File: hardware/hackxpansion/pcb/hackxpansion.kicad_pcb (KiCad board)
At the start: 4 copper layers, 52 x 65 mm, 101 parts, among them CN1 533981471, CN2 533981471, CN3 533981471, CN4 533981471, IC1 ADS7128IRTET, J1 Conn_01x03_MountingPin, J2 USB_C_Receptacle_USB2.0_14P, Q1 BSS138, Q2 2N7002, SW1 SW_Push, SW2 SW_Push, SW3 SW_On_Off, U2 RP2354B, U5 SPX3819M5-L-3-3, U7 BQ24075RGT, U8 USBLC6-2SC6, Y1 ABM8-272-T3

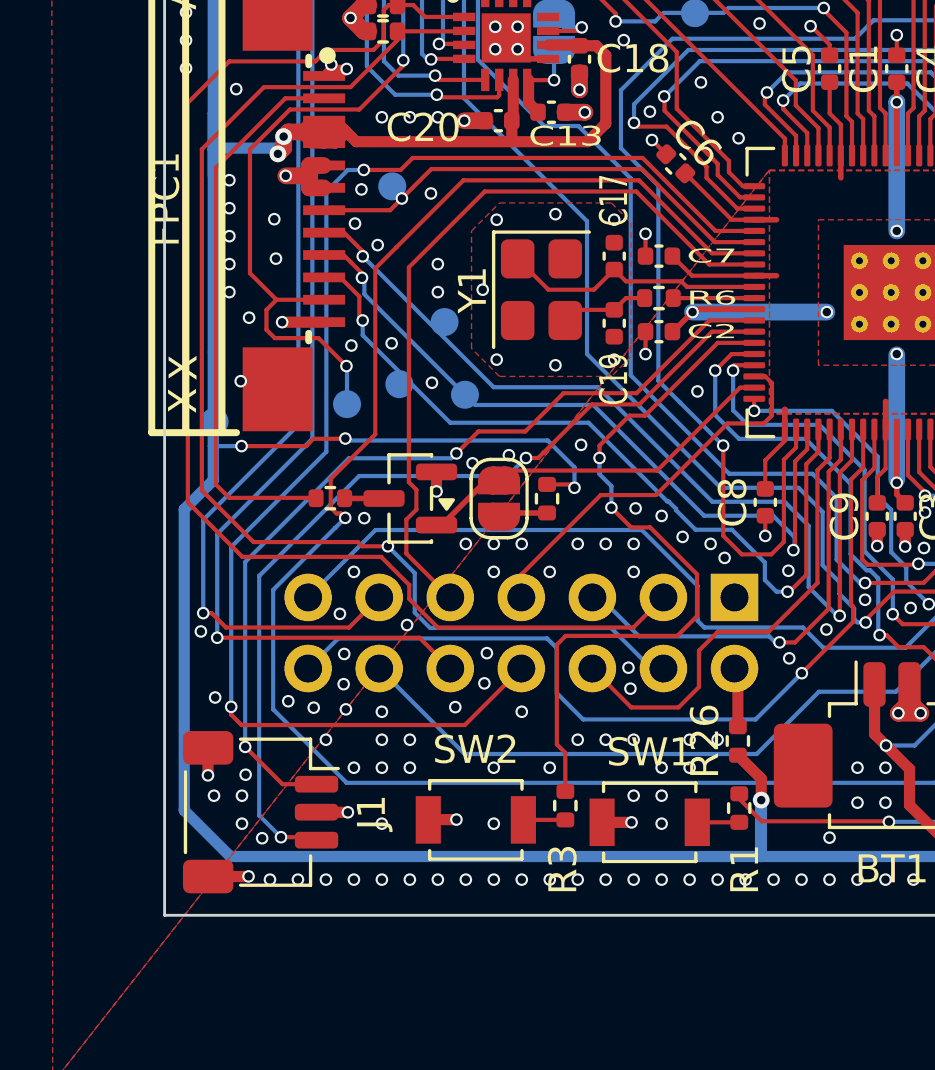
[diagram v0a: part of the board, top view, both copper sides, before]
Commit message: updated debug connector to standard 2x5 1.27mm
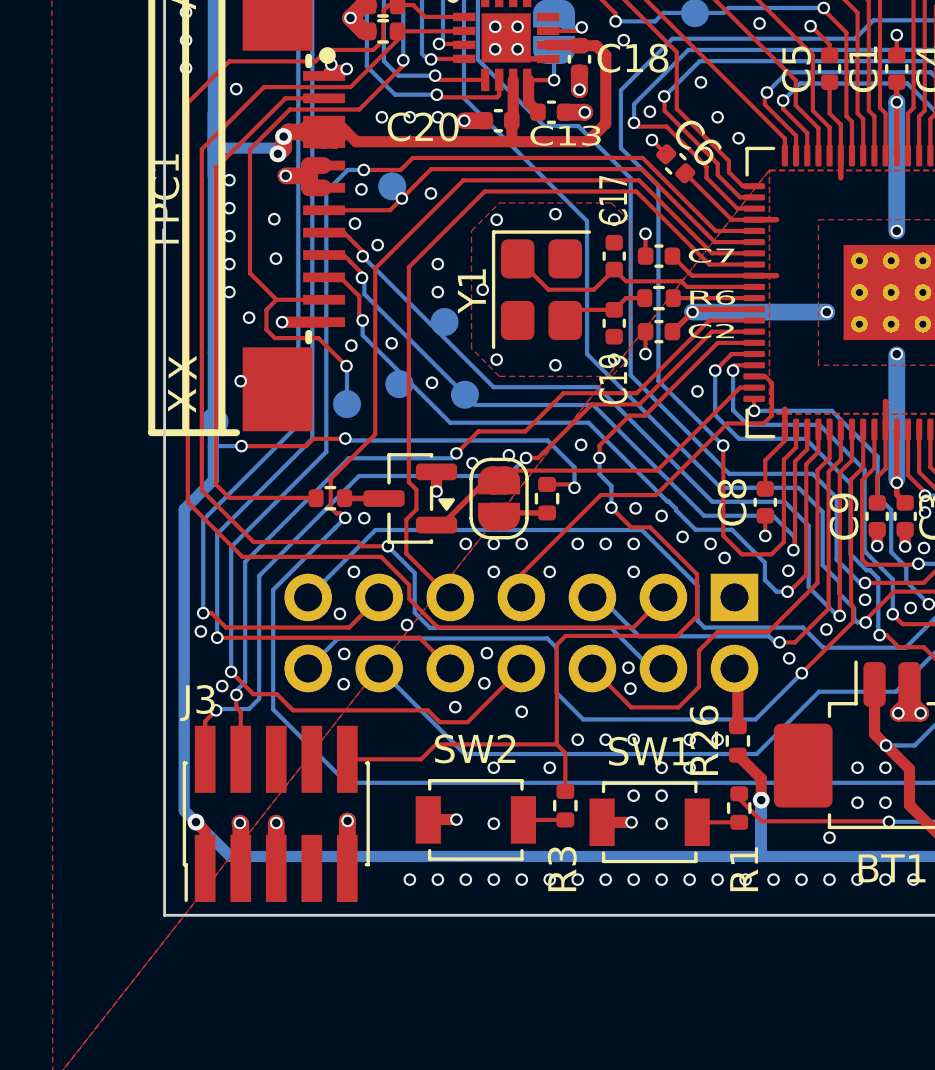
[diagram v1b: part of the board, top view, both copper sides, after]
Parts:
- removed J1: Conn_01x03_MountingPin, Connector_JST:JST_SH_SM03B-SRSS-TB_1x03-1MP_P1.00mm_Horizontal
- added J3: Conn_ARM_JTAG_SWD_10, Connector_PinHeader_1.27mm:PinHeader_2x05_P1.27mm_Vertical_SMD, F.Cu at (105.9, 97.3)
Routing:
- net /Main Board/RP2354B/RUN: track 25.8 -> 33.5 mm
- net /Main Board/RP2354B/SWDIO: track 32.3 -> 29.3 mm
- net /Main Board/RP2354B/SWCLK: track 31.5 -> 29.0 mm
- net /+3V3: track 295.6 -> 297.4 mm, vias 15 -> 16
- net /GND: track 64.4 -> 65.8 mm, vias 438 -> 417
- net /Main Board/Module Bay 0/GPIO3: track 48.3 -> 47.4 mm

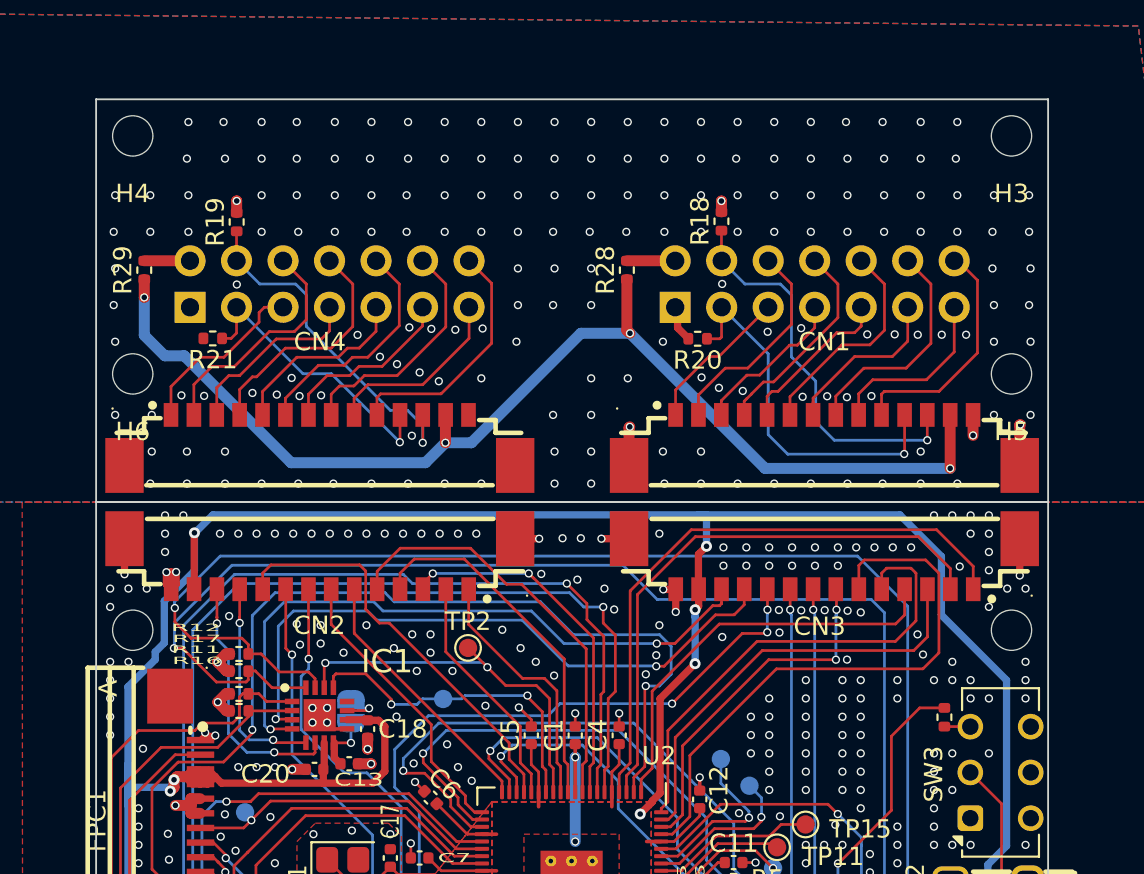
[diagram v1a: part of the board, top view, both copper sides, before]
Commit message: added silkscreen
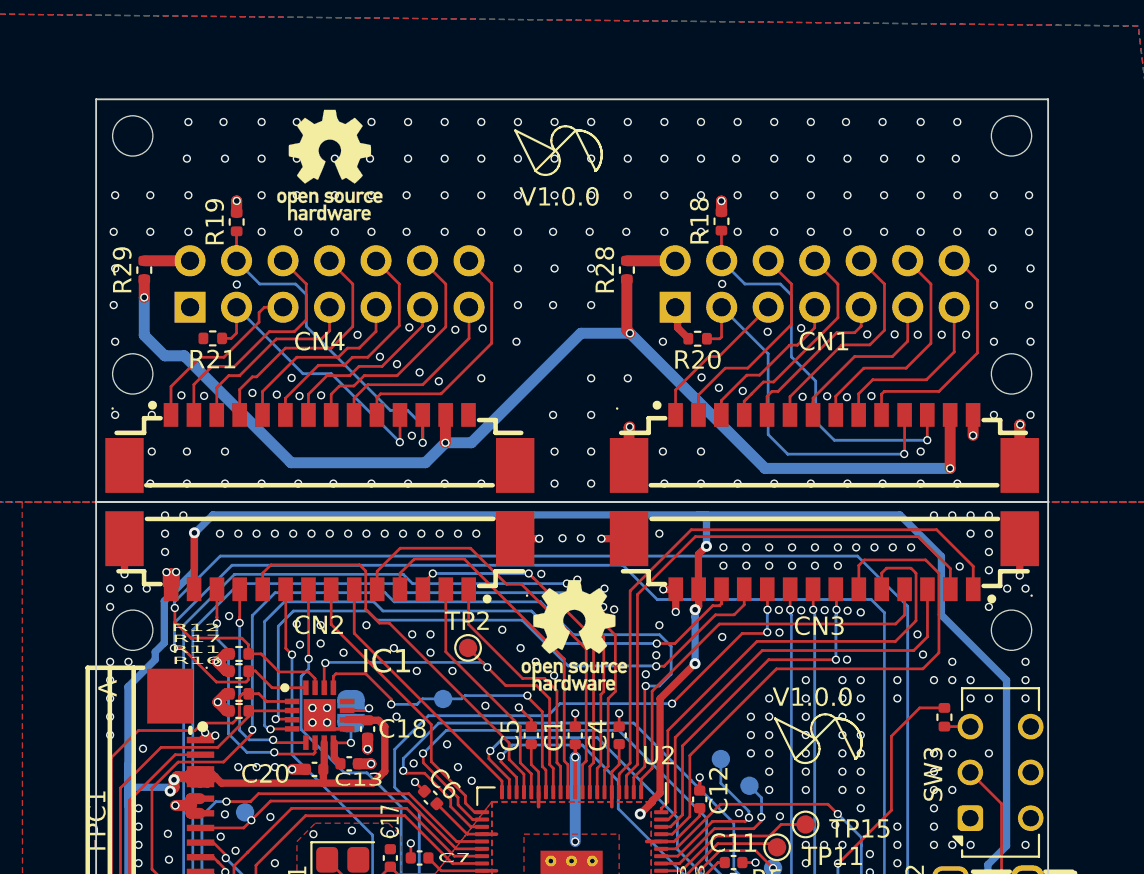
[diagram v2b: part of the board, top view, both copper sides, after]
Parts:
- added SYM1: Logo_Open_Hardware_Small, Symbol:OSHW-Logo_5.7x6mm_SilkScreen, F.Cu at (128.0, 65.2)
- added SYM2: Logo_Open_Hardware_Small, Symbol:OSHW-Logo_5.7x6mm_SilkScreen, F.Cu at (114.6, 39.5)
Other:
- board text added: "Mentions: - Simon - Hack Club - KiCAD discord - r/PrintedCircuitBoard"
- board text added: "V1.0.0"

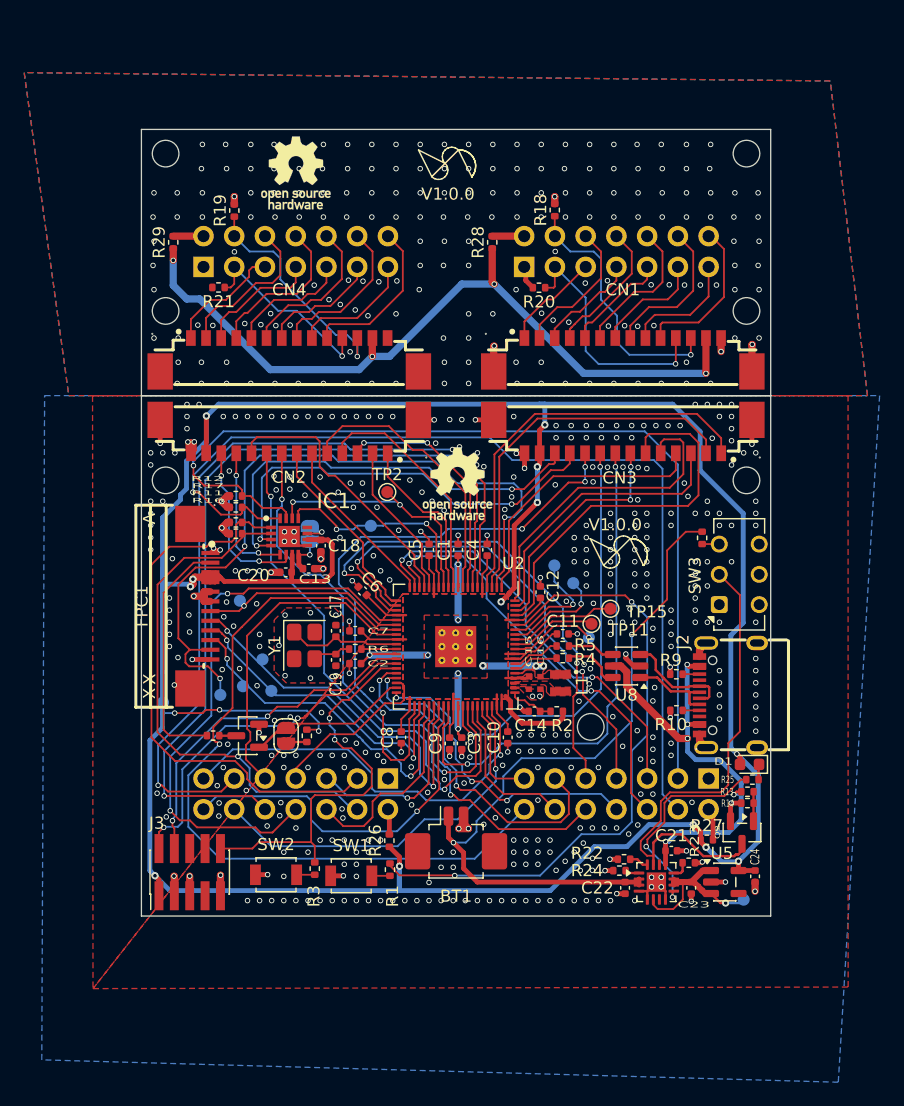
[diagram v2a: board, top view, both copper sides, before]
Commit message: unpaneled the two pcbs
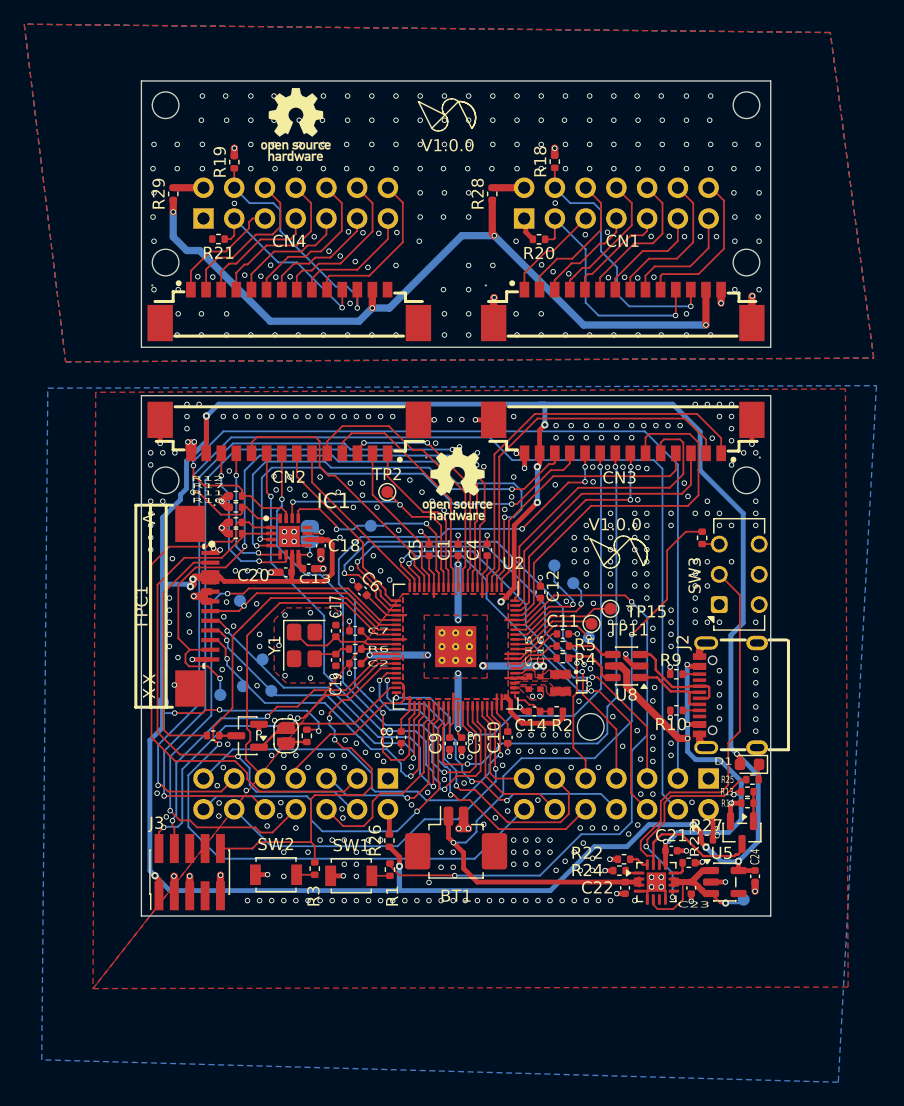
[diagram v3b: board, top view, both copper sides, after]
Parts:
- moved CN1 4.00 mm to (141.6, 50.5)
- moved CN4 4.00 mm to (114.1, 50.5)
- moved H3 4.00 mm to (151.9, 33.9)
- moved H4 4.00 mm to (103.9, 33.9)
- moved H5 4.00 mm to (151.9, 46.9)
- moved H6 4.00 mm to (103.9, 46.9)
- moved R18 4.00 mm to (136.0, 38.6)
- moved R19 4.00 mm to (109.5, 38.6)
- moved R20 4.00 mm to (134.7, 45.0)
- moved R21 4.00 mm to (108.2, 45.0)
- moved R28 4.00 mm to (130.9, 41.2)
- moved R29 4.00 mm to (104.5, 41.2)
- moved SYM2 4.00 mm to (114.6, 35.5)
- moved U4 4.00 mm to (133.5, 43.3)
- moved U6 4.00 mm to (107.0, 43.3)
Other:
- board size 52 x 65 mm -> 52 x 69 mm
